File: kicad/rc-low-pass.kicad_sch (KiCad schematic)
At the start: 11 parts, among them J1 Out, SW1 LEVEL 1, SW2 LEVEL 2, SW3 LEVEL 3

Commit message: add input voltage
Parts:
- added J2: In, TerminalBlock_Phoenix:TerminalBlock_Phoenix_MKDS-1,5-2-5.08_1x02_P5.08mm_Horizontal, symbol Connector:Conn_01x02_Female
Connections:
- net GND1: now also J2.1 (Pin_1)
- net VOLTAGE_IN: now reaches A1.30 (VIN)
- net VOLTAGE_IN: now also J2.2 (Pin_2)
- no-connect marks 26 -> 25
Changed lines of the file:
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@@
   (no_connect (at 157.48 86.36))
   (no_connect (at 182.88 93.98))
-  (no_connect (at 167.64 53.34))
   (no_connect (at 182.88 83.82))
   (no_connect (at 172.72 53.34))
@@
     (stroke (width 0) (type default) (color 0 0 0 0))
   )
+  (wire (pts (xy 201.93 55.88) (xy 208.28 55.88))
+    (stroke (width 0) (type default) (color 0 0 0 0))
+  )
   (wire (pts (xy 175.26 106.68) (xy 175.26 104.14))
     (stroke (width 0) (type default) (color 0 0 0 0))
@@
   )
   (wire (pts (xy 107.95 99.06) (xy 110.49 99.06))
+    (stroke (width 0) (type default) (color 0 0 0 0))
+  )
+  (wire (pts (xy 208.28 58.42) (xy 208.28 60.96))
     (stroke (width 0) (type default) (color 0 0 0 0))
   )
@@
     (property "Intersheet References" "${INTERSHEET_REFS}" (id 0) (at 147.0117 55.8006 0)
       (effects (font (size 1.27 1.27)) (justify left) hide)
+    )
+  )
+  (global_label "VOLTAGE_IN" (shape input) (at 167.64 53.34 90) (fields_autoplaced)
+    (effects (font (size 1.27 1.27)) (justify left))
+    (property "Intersheet References" "${INTERSHEET_REFS}" (id 0) (at 167.5606 40.1017 90)
+      (effects (font (size 1.27 1.27)) (justify left) hide)
+    )
+  )
+  (global_label "VOLTAGE_IN" (shape input) (at 208.28 60.96 180) (fields_autoplaced)
+    (effects (font (size 1.27 1.27)) (justify right))
+    (property "Intersheet References" "${INTERSHEET_REFS}" (id 0) (at 195.0417 61.0394 0)
+      (effects (font (size 1.27 1.27)) (justify right) hide)
     )
   )
@@
     (pin "2")
   )
+  (symbol (lib_id "Connector:Conn_01x02_Female") (at 213.36 55.88 0) (unit 1)
+    (in_bom yes) (on_board yes) (fields_autoplaced)
+    (property "Reference" "J2" (id 0) (at 214.63 55.8799 0)
+      (effects (font (size 1.27 1.27)) (justify left))
+    )
+    (property "Value" "In" (id 1) (at 214.63 58.4199 0)
+      (effects (font (size 1.27 1.27)) (justify left))
+    )
+    (property "Footprint" "TerminalBlock_Phoenix:TerminalBlock_Phoenix_MKDS-1,5-2-5.08_1x02_P5.08mm_Horizontal" (id 2) (at 213.36 55.88 0)
+      (effects (font (size 1.27 1.27)) hide)
+    )
+    (property "Datasheet" "~" (id 3) (at 213.36 55.88 0)
+      (effects (font (size 1.27 1.27)) hide)
+    )
+    (pin "1")
+    (pin "2")
+  )
   (symbol (lib_id "power:GND") (at 125.73 71.12 0) (unit 1)
     (in_bom yes) (on_board yes) (fields_autoplaced)
@@
     (pin "2")
   )
+  (symbol (lib_id "power:GND1") (at 201.93 55.88 0) (unit 1)
+    (in_bom yes) (on_board yes)
+    (property "Reference" "#PWR0106" (id 0) (at 201.93 62.23 0)
+      (effects (font (size 1.27 1.27)) hide)
+    )
+    (property "Value" "GND1" (id 1) (at 198.12 57.15 0))
+    (property "Footprint" "" (id 2) (at 201.93 55.88 0)
+      (effects (font (size 1.27 1.27)) hide)
+    )
+    (property "Datasheet" "" (id 3) (at 201.93 55.88 0)
+      (effects (font (size 1.27 1.27)) hide)
+    )
+    (pin "1")
+  )
   (symbol (lib_id "power:GND") (at 170.18 106.68 0) (unit 1)
     (in_bom yes) (on_board yes) (fields_autoplaced)
@@
       (reference "#PWR0105") (unit 1) (value "GND1") (footprint "")
     )
+    (path "/c37dcd1e-d55c-4ea2-9efb-cab1bfceffbc"
+      (reference "#PWR0106") (unit 1) (value "GND1") (footprint "")
+    )
     (path "/3cf8263f-9348-4de3-8e55-22d349486a35"
       (reference "A1") (unit 1) (value "Arduino Nano") (footprint "Module:Arduino_Nano")
@@
       (reference "J1") (unit 1) (value "Out") (footprint "TerminalBlock_Phoenix:TerminalBlock_Phoenix_MKDS-1,5-2-5.08_1x02_P5.08mm_Horizontal")
     )
+    (path "/692dffb0-eeb3-460d-80d8-8bd9541d6d51"
+      (reference "J2") (unit 1) (value "In") (footprint "TerminalBlock_Phoenix:TerminalBlock_Phoenix_MKDS-1,5-2-5.08_1x02_P5.08mm_Horizontal")
+    )
     (path "/ce1d4c31-a2d4-4852-849e-0e281377f354"

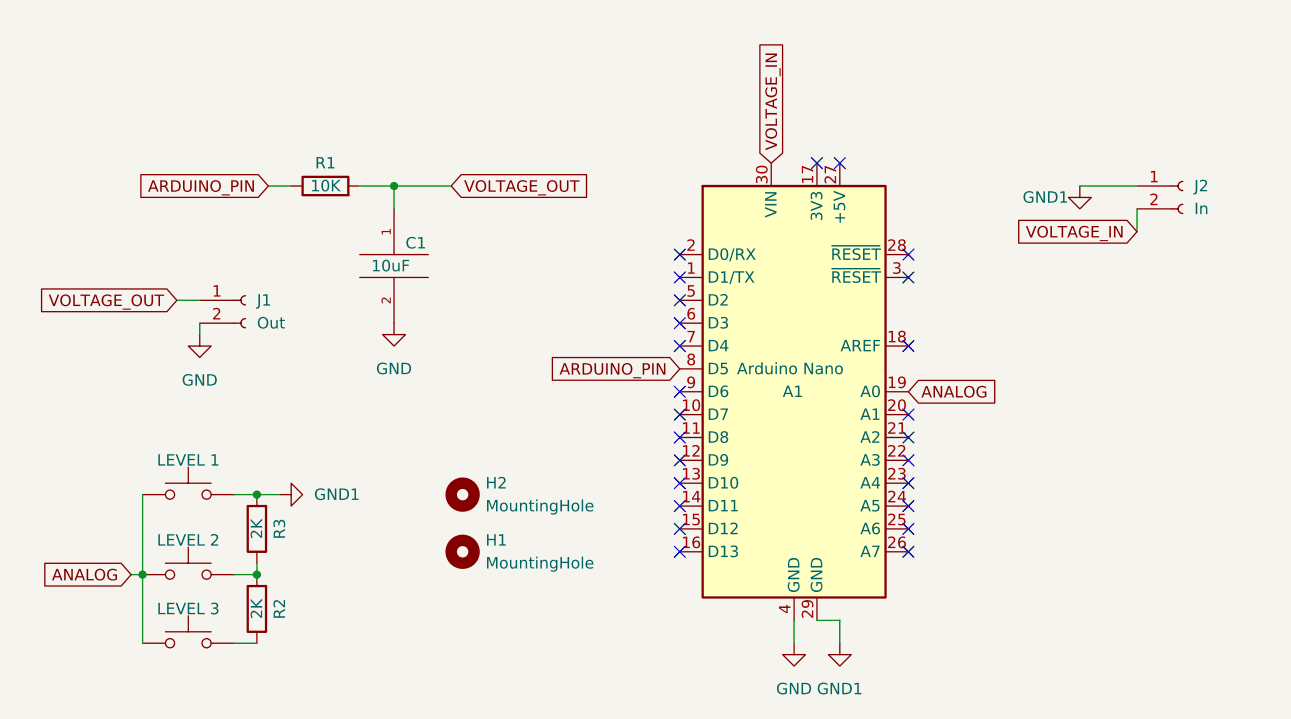
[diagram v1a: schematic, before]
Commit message: add led indicators of levels
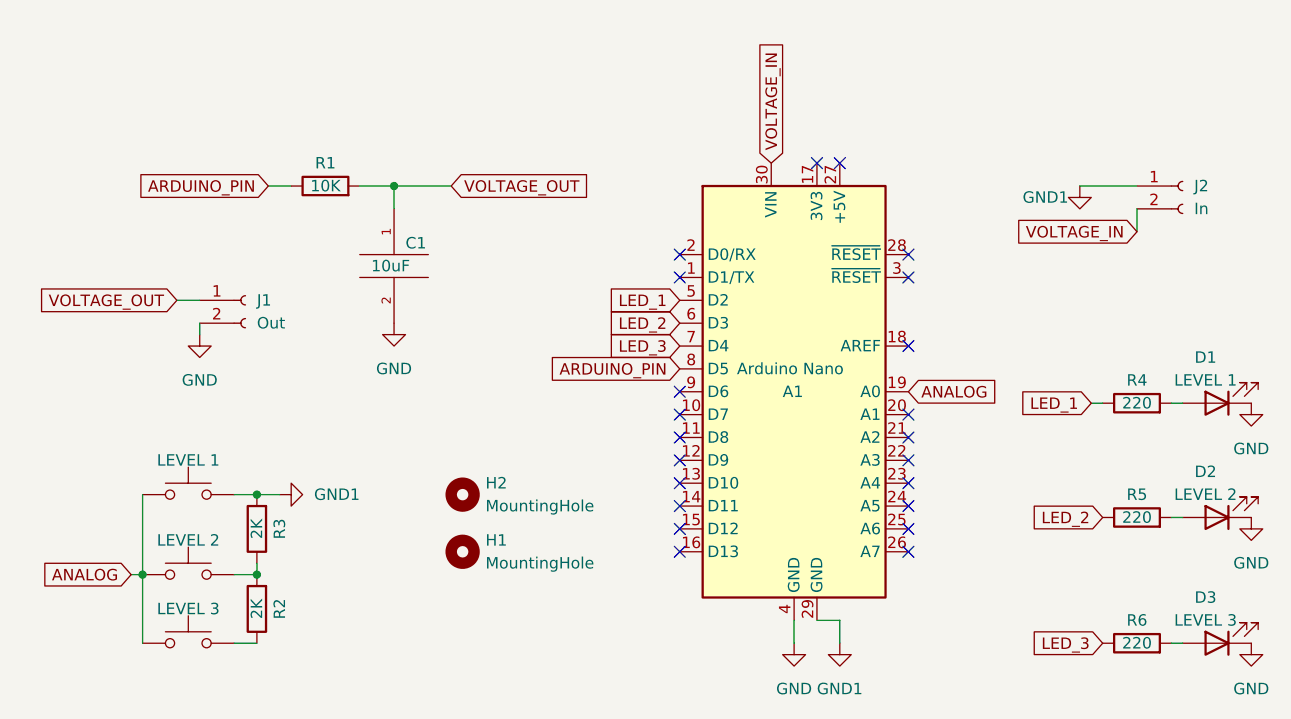
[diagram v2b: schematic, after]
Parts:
- added D1: LEVEL 1, LED_THT:LED_D5.0mm, symbol Device:LED
- added D2: LEVEL 2, LED_THT:LED_D5.0mm, symbol Device:LED
- added D3: LEVEL 3, LED_THT:LED_D5.0mm, symbol Device:LED
- added R4, R5, R6: 220, Resistor_THT:R_Axial_DIN0411_L9.9mm_D3.6mm_P12.70mm_Horizontal, symbol Device:R
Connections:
- net GND: now also D1.1 (K), D2.1 (K), D3.1 (K)
- net LED_1: now reaches A1.5 (D2)
- net LED_1: now also R4.1
- net LED_2: now reaches A1.6 (D3)
- net LED_2: now also R5.1
- net LED_3: now reaches A1.7 (D4)
- net LED_3: now also R6.1
- new net: D2.2 (A), R5.2
- new net: D3.2 (A), R6.2
- new net: D1.2 (A), R4.2
- no-connect marks 25 -> 22
